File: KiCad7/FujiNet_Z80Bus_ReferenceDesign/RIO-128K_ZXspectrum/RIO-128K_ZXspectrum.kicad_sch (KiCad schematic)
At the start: 6 parts

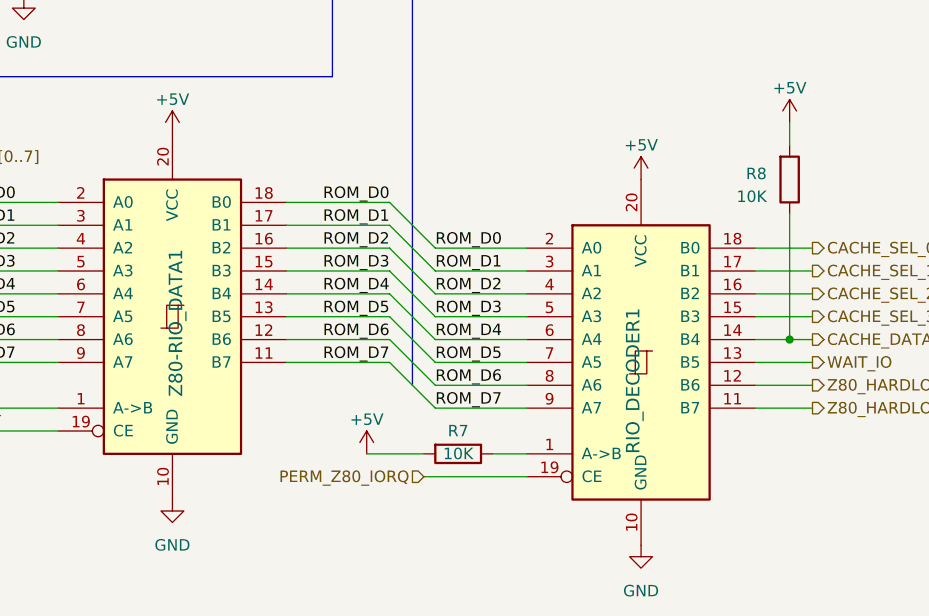
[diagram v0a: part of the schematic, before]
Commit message: KiCad - Refactoring RIO IOCACHE to projects
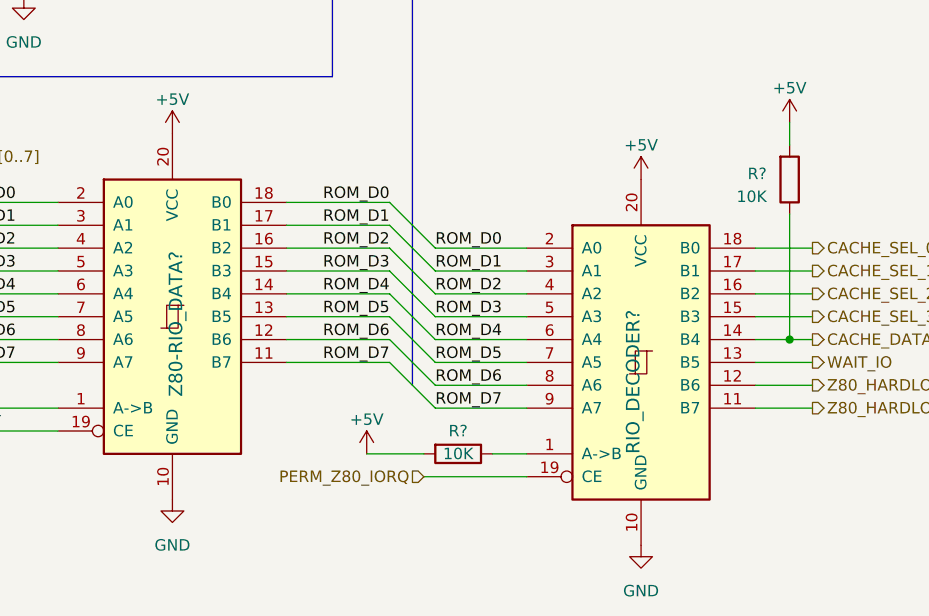
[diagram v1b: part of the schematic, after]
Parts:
- renumbered R7 to R?, R8 to R?, RIO_DECODER1 to RIO_DECODER?, Z80-RIO_DATA1 to Z80-RIO_DATA?
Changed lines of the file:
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@@
   (symbol (lib_id "74xx:74HC245") (at 191.77 127 0) (unit 1)
     (in_bom yes) (on_board yes) (dnp no)
-    (property "Reference" "RIO_DECODER1" (at 191.77 137.16 90)
+    (property "Reference" "RIO_DECODER?" (at 191.77 137.16 90)
       (effects (font (size 1.4986 1.4986)) (justify left bottom))
     )
@@
     (instances
       (project "FujiNet_Z80Bus_ReferenceDesign"
-        (path "/532c0392-800e-45cc-8170-6d32f2390e83/00000000-0000-0000-0000-0000ad721c5e"
-          (reference "RIO_DECODER1") (unit 1)
-        )
         (path "/532c0392-800e-45cc-8170-6d32f2390e83"
           (reference "RIO_DECODER?") (unit 1)
@@
           (reference "RIO_DECODER?") (unit 1)
         )
+        (path "/532c0392-800e-45cc-8170-6d32f2390e83/00000000-0000-0000-0000-0000ad721c5e"
+          (reference "RIO_DECODER1") (unit 1)
+        )
       )
     )
@@
   (symbol (lib_id "Device:R") (at 171.45 137.16 270) (unit 1)
     (in_bom yes) (on_board yes) (dnp no) (fields_autoplaced)
-    (property "Reference" "R7" (at 171.45 134.62 90)
+    (property "Reference" "R?" (at 171.45 134.62 90)
       (effects (font (size 1.27 1.27)))
     )
@@
     (instances
       (project "FujiNet_Z80Bus_ReferenceDesign"
-        (path "/532c0392-800e-45cc-8170-6d32f2390e83/00000000-0000-0000-0000-0000ad721c5e"
-          (reference "R7") (unit 1)
-        )
         (path "/532c0392-800e-45cc-8170-6d32f2390e83/00000000-0000-0000-0000-0000ae2cbb6b"
           (reference "R?") (unit 1)
         )
+        (path "/532c0392-800e-45cc-8170-6d32f2390e83/00000000-0000-0000-0000-0000ad721c5e"
+          (reference "R7") (unit 1)
+        )
       )
     )
@@
   (symbol (lib_id "74xx:74HC245") (at 139.7 121.92 0) (unit 1)
     (in_bom yes) (on_board yes) (dnp no)
-    (property "Reference" "Z80-RIO_DATA1" (at 140.97 130.81 90)
+    (property "Reference" "Z80-RIO_DATA?" (at 140.97 130.81 90)
       (effects (font (size 1.4986 1.4986)) (justify left bottom))
     )
@@
     (instances
       (project "FujiNet_Z80Bus_ReferenceDesign"
-        (path "/532c0392-800e-45cc-8170-6d32f2390e83/00000000-0000-0000-0000-0000ad721c5e"
-          (reference "Z80-RIO_DATA1") (unit 1)
-        )
         (path "/532c0392-800e-45cc-8170-6d32f2390e83"
           (reference "Z80-RIO_DATA?") (unit 1)
         )
+        (path "/532c0392-800e-45cc-8170-6d32f2390e83/00000000-0000-0000-0000-0000ad721c5e"
+          (reference "Z80-RIO_DATA1") (unit 1)
+        )
       )
     )
@@
   (symbol (lib_id "power:+5V") (at 191.77 106.68 0) (unit 1)
     (in_bom yes) (on_board yes) (dnp no) (fields_autoplaced)
-    (property "Reference" "#PWR055" (at 191.77 110.49 0)
+    (property "Reference" "#PWR025" (at 191.77 110.49 0)
       (effects (font (size 1.27 1.27)) hide)
     )
@@
     (instances
       (project "FujiNet_Z80Bus_ReferenceDesign"
-        (path "/532c0392-800e-45cc-8170-6d32f2390e83/00000000-0000-0000-0000-0000ad721c5e"
-          (reference "#PWR055") (unit 1)
-        )
         (path "/532c0392-800e-45cc-8170-6d32f2390e83/6a1fd481-1635-4a64-b244-c204161ad407"
           (reference "#PWR025") (unit 1)
+        )
+        (path "/532c0392-800e-45cc-8170-6d32f2390e83/00000000-0000-0000-0000-0000ad721c5e"
+          (reference "#PWR055") (unit 1)
         )
       )
@@
   (symbol (lib_id "power:+5V") (at 139.7 101.6 0) (unit 1)
     (in_bom yes) (on_board yes) (dnp no) (fields_autoplaced)
-    (property "Reference" "#PWR060" (at 139.7 105.41 0)
+    (property "Reference" "#PWR025" (at 139.7 105.41 0)
       (effects (font (size 1.27 1.27)) hide)
     )
@@
     (instances
       (project "FujiNet_Z80Bus_ReferenceDesign"
-        (path "/532c0392-800e-45cc-8170-6d32f2390e83/00000000-0000-0000-0000-0000ad721c5e"
-          (reference "#PWR060") (unit 1)
-        )
         (path "/532c0392-800e-45cc-8170-6d32f2390e83/6a1fd481-1635-4a64-b244-c204161ad407"
           (reference "#PWR025") (unit 1)
         )
+        (path "/532c0392-800e-45cc-8170-6d32f2390e83/00000000-0000-0000-0000-0000ad721c5e"
+          (reference "#PWR060") (unit 1)
+        )
       )
     )
@@
   (symbol (lib_id "Device:R") (at 208.28 106.68 0) (mirror x) (unit 1)
     (in_bom yes) (on_board yes) (dnp no) (fields_autoplaced)
-    (property "Reference" "R8" (at 205.74 106.045 0)
+    (property "Reference" "R?" (at 205.74 106.045 0)
       (effects (font (size 1.27 1.27)) (justify right))
     )
@@
     (instances
       (project "FujiNet_Z80Bus_ReferenceDesign"
-        (path "/532c0392-800e-45cc-8170-6d32f2390e83/00000000-0000-0000-0000-0000ad721c5e"
-          (reference "R8") (unit 1)
-        )
         (path "/532c0392-800e-45cc-8170-6d32f2390e83/00000000-0000-0000-0000-0000ae2cbb6b"
           (reference "R?") (unit 1)
@@
           (reference "R6") (unit 1)
         )
+        (path "/532c0392-800e-45cc-8170-6d32f2390e83/00000000-0000-0000-0000-0000ad721c5e"
+          (reference "R8") (unit 1)
+        )
       )
     )
@@
   (symbol (lib_id "power:+5V") (at 208.28 100.33 0) (unit 1)
     (in_bom yes) (on_board yes) (dnp no) (fields_autoplaced)
-    (property "Reference" "#PWR022" (at 208.28 104.14 0)
+    (property "Reference" "#PWR025" (at 208.28 104.14 0)
       (effects (font (size 1.27 1.27)) hide)
     )
@@
     (instances
       (project "FujiNet_Z80Bus_ReferenceDesign"
-        (path "/532c0392-800e-45cc-8170-6d32f2390e83/00000000-0000-0000-0000-0000ad721c5e"
-          (reference "#PWR022") (unit 1)
-        )
         (path "/532c0392-800e-45cc-8170-6d32f2390e83/6a1fd481-1635-4a64-b244-c204161ad407"
           (reference "#PWR025") (unit 1)
         )
-      )
+        (path "/532c0392-800e-45cc-8170-6d32f2390e83/00000000-0000-0000-0000-0000ad721c5e"
+          (reference "#PWR022") (unit 1)
+        )
+      )

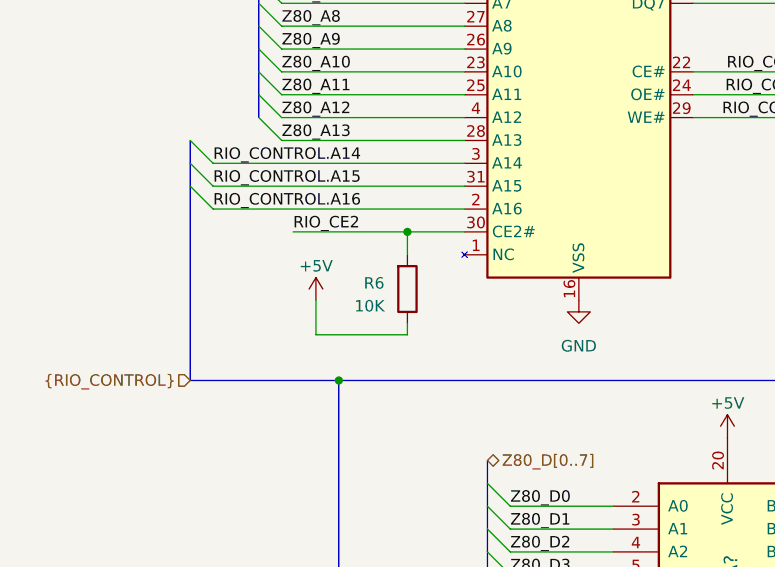
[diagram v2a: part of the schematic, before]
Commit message: KiCad - Refactored the SPI bus
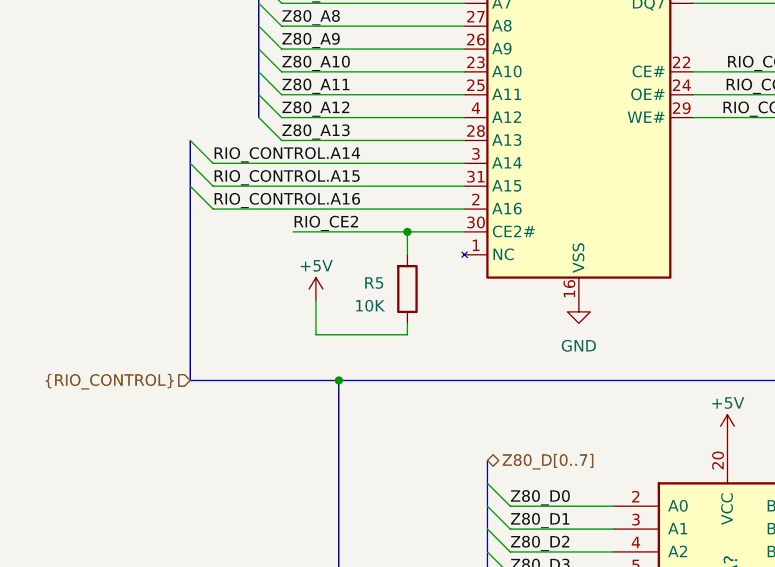
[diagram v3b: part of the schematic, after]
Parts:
- renumbered R6 to R5
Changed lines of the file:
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@@
   (symbol (lib_id "Device:R") (at 104.14 85.09 0) (mirror x) (unit 1)
     (in_bom yes) (on_board yes) (dnp no) (fields_autoplaced)
-    (property "Reference" "R6" (at 101.6 84.455 0)
+    (property "Reference" "R5" (at 101.6 84.455 0)
       (effects (font (size 1.27 1.27)) (justify right))
     )
@@
       (project "FujiNet_Z80Bus_ReferenceDesign"
         (path "/532c0392-800e-45cc-8170-6d32f2390e83/00000000-0000-0000-0000-0000ad721c5e"
-          (reference "R6") (unit 1)
+          (reference "R5") (unit 1)
         )
       )
@@
   (symbol (lib_id "power:GND") (at 123.19 86.36 0) (unit 1)
     (in_bom yes) (on_board yes) (dnp no) (fields_autoplaced)
-    (property "Reference" "#PWR048" (at 123.19 92.71 0)
+    (property "Reference" "#PWR044" (at 123.19 92.71 0)
       (effects (font (size 1.27 1.27)) hide)
     )
@@
       (project "FujiNet_Z80Bus_ReferenceDesign"
         (path "/532c0392-800e-45cc-8170-6d32f2390e83/00000000-0000-0000-0000-0000ad721c5e"
-          (reference "#PWR048") (unit 1)
+          (reference "#PWR044") (unit 1)
         )
       )
@@
         )
         (path "/532c0392-800e-45cc-8170-6d32f2390e83/00000000-0000-0000-0000-0000ad721c5e"
-          (reference "R7") (unit 1)
+          (reference "R6") (unit 1)
         )
       )
@@
   (symbol (lib_id "power:+5V") (at 161.29 137.16 0) (unit 1)
     (in_bom yes) (on_board yes) (dnp no) (fields_autoplaced)
-    (property "Reference" "#PWR051" (at 161.29 140.97 0)
+    (property "Reference" "#PWR047" (at 161.29 140.97 0)
       (effects (font (size 1.27 1.27)) hide)
     )
@@
       (project "FujiNet_Z80Bus_ReferenceDesign"
         (path "/532c0392-800e-45cc-8170-6d32f2390e83/00000000-0000-0000-0000-0000ad721c5e"
-          (reference "#PWR051") (unit 1)
+          (reference "#PWR047") (unit 1)
         )
       )
@@
   (symbol (lib_id "power:+5V") (at 123.19 30.48 0) (unit 1)
     (in_bom yes) (on_board yes) (dnp no) (fields_autoplaced)
-    (property "Reference" "#PWR047" (at 123.19 34.29 0)
+    (property "Reference" "#PWR043" (at 123.19 34.29 0)
       (effects (font (size 1.27 1.27)) hide)
     )
@@
       (project "FujiNet_Z80Bus_ReferenceDesign"
         (path "/532c0392-800e-45cc-8170-6d32f2390e83/00000000-0000-0000-0000-0000ad721c5e"
-          (reference "#PWR047") (unit 1)
+          (reference "#PWR043") (unit 1)
         )
       )
@@
         )
         (path "/532c0392-800e-45cc-8170-6d32f2390e83/00000000-0000-0000-0000-0000ad721c5e"
-          (reference "#PWR052") (unit 1)
+          (reference "#PWR048") (unit 1)
         )
       )
@@
   (symbol (lib_id "power:GND") (at 191.77 147.32 0) (unit 1)
     (in_bom yes) (on_board yes) (dnp no) (fields_autoplaced)
-    (property "Reference" "#PWR053" (at 191.77 153.67 0)
+    (property "Reference" "#PWR049" (at 191.77 153.67 0)
       (effects (font (size 1.27 1.27)) hide)
     )
@@
       (project "FujiNet_Z80Bus_ReferenceDesign"
         (path "/532c0392-800e-45cc-8170-6d32f2390e83/00000000-0000-0000-0000-0000ad721c5e"
-          (reference "#PWR053") (unit 1)
+          (reference "#PWR049") (unit 1)
         )
       )
@@
         )
         (path "/532c0392-800e-45cc-8170-6d32f2390e83/00000000-0000-0000-0000-0000ad721c5e"
-          (reference "#PWR049") (unit 1)
+          (reference "#PWR045") (unit 1)
         )
       )
@@
   (symbol (lib_id "power:+5V") (at 93.98 86.36 0) (mirror y) (unit 1)
     (in_bom yes) (on_board yes) (dnp no) (fields_autoplaced)
-    (property "Reference" "#PWR046" (at 93.98 90.17 0)
+    (property "Reference" "#PWR042" (at 93.98 90.17 0)
       (effects (font (size 1.27 1.27)) hide)
     )
@@
       (project "FujiNet_Z80Bus_ReferenceDesign"
         (path "/532c0392-800e-45cc-8170-6d32f2390e83/00000000-0000-0000-0000-0000ad721c5e"
-          (reference "#PWR046") (unit 1)
+          (reference "#PWR042") (unit 1)
         )
       )
@@
         )
         (path "/532c0392-800e-45cc-8170-6d32f2390e83/00000000-0000-0000-0000-0000ad721c5e"
-          (reference "R8") (unit 1)
+          (reference "R7") (unit 1)
         )
       )
@@
         )
         (path "/532c0392-800e-45cc-8170-6d32f2390e83/00000000-0000-0000-0000-0000ad721c5e"
-          (reference "#PWR054") (unit 1)
+          (reference "#PWR050") (unit 1)
         )
       )
@@
   (symbol (lib_id "power:GND") (at 139.7 142.24 0) (unit 1)
     (in_bom yes) (on_board yes) (dnp no) (fields_autoplaced)
-    (property "Reference" "#PWR050" (at 139.7 148.59 0)
+    (property "Reference" "#PWR046" (at 139.7 148.59 0)
       (effects (font (size 1.27 1.27)) hide)
     )
@@
       (project "FujiNet_Z80Bus_ReferenceDesign"
         (path "/532c0392-800e-45cc-8170-6d32f2390e83/00000000-0000-0000-0000-0000ad721c5e"
-          (reference "#PWR050") (unit 1)
-        )
-      )
+          (reference "#PWR046") (unit 1)
+        )
+      )

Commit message: KiCad - Proof of concept PCB in-progress
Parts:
- RIO1: footprint Package_DIP:DIP-32_W15.24mm -> Package_DIP:DIP-32_W15.24mm_Socket
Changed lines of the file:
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@@
     (rev "0.1")
     (company "FujiNet")
+    (comment 2 "each bytes address relates to a Z80 IO address")
+    (comment 3 "RIO has 64K of RAM which is programmed with an IO configuration byte")
+    (comment 4 "RIO emulates a ROM (4K@0000h) and Decodes IO address")
   )
   (bus_alias "RIO_CONTROL" (members "RIO_CONTROL.A16" "RIO_CONTROL.A15" "RIO_CONTROL.A14" "RIO_CONTROL.A13" "RIO_CONTROL.WE" "RIO_CONTROL.CE" "RIO_CONTROL.OE" "RIO_CONTROL.ROM_RDY"))
@@
       (effects (font (size 1.27 1.27)) (justify left))
     )
-    (property "Footprint" "Package_DIP:DIP-32_W15.24mm" (at 123.19 55.88 0)
-      (effects (font (size 1.27 1.27)) hide)
-    )
+    (property "Footprint" "Package_DIP:DIP-32_W15.24mm_Socket" (at 123.19 55.88 0)
+      (effects (font (size 1.27 1.27)) hide)
+    )
